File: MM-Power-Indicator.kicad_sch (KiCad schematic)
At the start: 2 parts

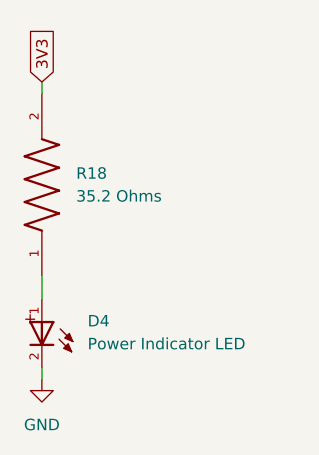
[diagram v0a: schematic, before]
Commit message: finished adding rest of footprints, tried replacing mosfets with no success
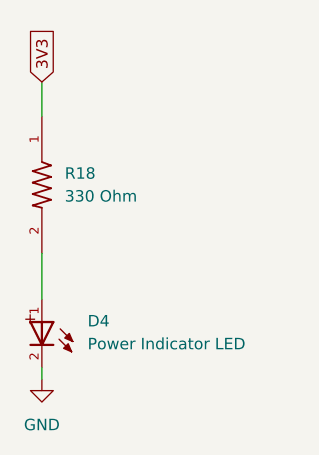
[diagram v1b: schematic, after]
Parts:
- removed R18: 35.2 Ohms, RN73R1JTTD35R2B25:RESC1608X55N, symbol 35.2ohmResistor_RN73R1JTTD35R2B25:RN73R1JTTD35R2B25
- added R18: 330 Ohm, 330_ohm_RC0603FR-07330RL:RESC1607X60N, symbol 330_ohm_RC0603FR-07330RL:RC0603FR-07330RL
- D4: footprint WL-TMRC_5MM:WL-TMRC_5MM -> LED_WL-TMRC_5MM:WL-TMRC_5MM
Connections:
- net 3V3: now also R18.1
- net at D4.1: now also R18.2
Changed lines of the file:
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@@
 	(wire
 		(pts
-			(xy 132.08 97.79) (xy 132.08 100.33)
+			(xy 132.08 95.25) (xy 132.08 100.33)
 		)
 		(stroke
@@
 	(wire
 		(pts
-			(xy 132.08 76.2) (xy 132.08 77.47)
+			(xy 132.08 76.2) (xy 132.08 80.01)
 		)
 		(stroke
@@
 			)
 		)
-		(property "Footprint" "WL-TMRC_5MM:WL-TMRC_5MM"
+		(property "Footprint" "LED_WL-TMRC_5MM:WL-TMRC_5MM"
 			(at 132.08 105.41 0)
 			(effects
@@
 	)
 	(symbol
-		(lib_id "35.2ohmResistor_RN73R1JTTD35R2B25:RN73R1JTTD35R2B25")
-		(at 132.08 87.63 90)
+		(lib_id "330_ohm_RC0603FR-07330RL:RC0603FR-07330RL")
+		(at 132.08 87.63 270)
 		(unit 1)
 		(exclude_from_sim no)
@@
 		(fields_autoplaced yes)
 		(property "Reference" "R18"
-			(at 135.89 86.3599 90)
-			(effects
-				(font
-					(size 1.27 1.27)
-				)
-				(justify right)
-			)
-		)
-		(property "Value" "35.2 Ohms"
-			(at 135.89 88.8999 90)
-			(effects
-				(font
-					(size 1.27 1.27)
-				)
-				(justify right)
-			)
-		)
-		(property "Footprint" "RN73R1JTTD35R2B25:RESC1608X55N"
+			(at 134.62 86.3599 90)
+			(effects
+				(font
+					(size 1.27 1.27)
+				)
+				(justify left)
+			)
+		)
+		(property "Value" "330 Ohm"
+			(at 134.62 88.8999 90)
+			(effects
+				(font
+					(size 1.27 1.27)
+				)
+				(justify left)
+			)
+		)
+		(property "Footprint" "330_ohm_RC0603FR-07330RL:RESC1607X60N"
 			(at 132.08 87.63 0)
 			(effects
@@
 			)
 		)
+		(property "DigiKey_Part_Number" "311-330HRCT-ND"
+			(at 132.08 87.63 0)
+			(effects
+				(font
+					(size 1.27 1.27)
+				)
+				(justify bottom)
+				(hide yes)
+			)
+		)
+		(property "SnapEDA_Link" "https://www.snapeda.com/parts/RC0603FR-07330RL/Yageo/view-part/?ref=snap"
+			(at 132.08 87.63 0)
+			(effects
+				(font
+					(size 1.27 1.27)
+				)
+				(justify bottom)
+				(hide yes)
+			)
+		)
+		(property "Description_1" "330 Ohms ±1% 0.1W, 1/10W Chip Resistor 0603 (1608 Metric) Moisture Resistant Thick Film"
+			(at 132.08 87.63 0)
+			(effects
+				(font
+					(size 1.27 1.27)
+				)
+				(justify bottom)
+				(hide yes)
+			)
+		)
+		(property "MF" "Yageo"
+			(at 132.08 87.63 0)
+			(effects
+				(font
+					(size 1.27 1.27)
+				)
+				(justify bottom)
+				(hide yes)
+			)
+		)
+		(property "Package" "0603 Yageo"
+			(at 132.08 87.63 0)
+			(effects
+				(font
+					(size 1.27 1.27)
+				)
+				(justify bottom)
+				(hide yes)
+			)
+		)
+		(property "Check_prices" "https://www.snapeda.com/parts/RC0603FR-07330RL/Yageo/view-part/?ref=eda"
+			(at 132.08 87.63 0)
+			(effects
+				(font
+					(size 1.27 1.27)
+				)
+				(justify bottom)
+				(hide yes)
+			)
+		)
+		(property "MP" "RC0603FR-07330RL"
+			(at 132.08 87.63 0)
+			(effects
+				(font
+					(size 1.27 1.27)
+				)
+				(justify bottom)
+				(hide yes)
+			)
+		)
+		(pin "2"
+		)
 		(pin "1"
 		)
-		(pin "2"
-		)
 		(instances
